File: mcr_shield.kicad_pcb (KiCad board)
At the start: 2 copper layers, 135 x 95 mm, 23 parts, among them J2 MCR_P1_Controls, J3 MCR_System_Coin, J4 MCR_Opt_X_Dial, J5 MCR_P2_Controls, SW1 Game_Selector, SW2 Cabinet_Options, U1 Buck_Regulator, U2 Optocoupler_P1, U3 Optocoupler_Sys, U4 Sync_Buffer, U5 Audio_Amplifier

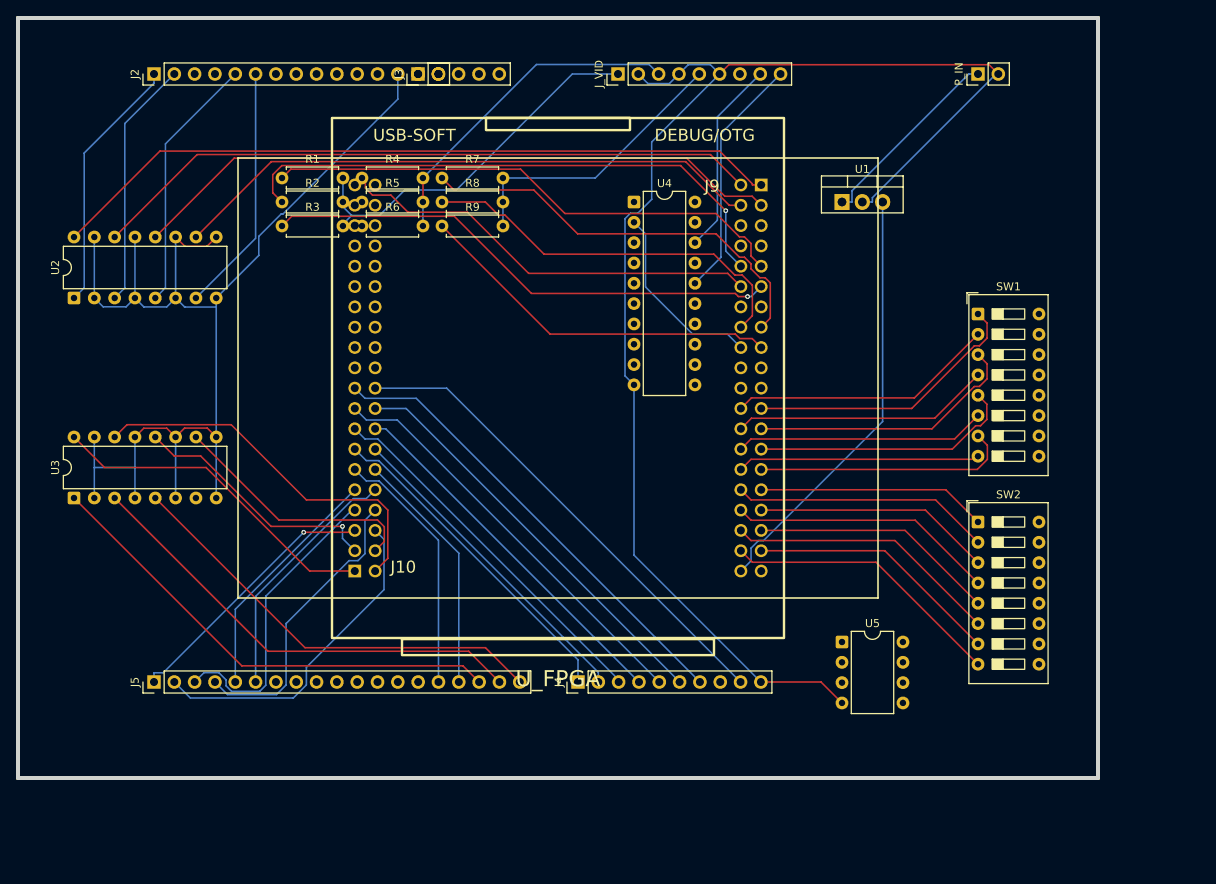
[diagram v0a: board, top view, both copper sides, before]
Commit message: Tang Console 60K bring-up: USB gamepad, multi-game configs, VGA out, DDR3 framebuffer (WIP)
Backport the working Primer 25K design to the Console 60K and grow it:

- Console 60K port verified on hardware: pins cross-checked against
  nand2mario nestang/snestang/gbatang and the Sipeed 32001A/C schematics
  (J10 header ball map extracted; docs/pinrefs/ carries the references).
- USB HID gamepad on USB port 1 (vendored nand2mario usb_hid_host + 12MHz
  PLLA); board keys act as reset/coin.
- Per-game build configs via merge_roms.py-generated game_config.vh:
  Domino Man, Tron (spinner via MiSTer spinner.sv on pad X/Y), Satan's
  Hollow - input/DIP maps verified against MAME mcr.cpp (incl. the Domino
  0x3E upright DIP fix). Flashables kept in bitstreams/.
- Analog VGA (PmodVGA or DE-15 breakout) from J10 with a 15/31kHz strap;
  PMOD-socket mapping straps pending hardware verification.
- DDR3 framebuffer HDMI path (vendored from gbatang, GPLv3): 512x480
  captured to on-SOM DDR3, upscaled to 1280x720@60 with HDMI audio.
  STATUS: builds clean, timing met, but no HDMI sync on hardware yet -
  under debug via new UART status beacon (U15 -> USB-C serial) and J10
  debug pins; gbatang-m60k reference bitstream staged as control test.
- Docs: CLAUDE.md, universal MCR shield spec (J10 pin table, net plan),
  machine-readable MCR game input matrix; Bank 9 1.5V constraint recorded.

Co-Authored-By: Claude Fable 5 <noreply@anthropic.com>
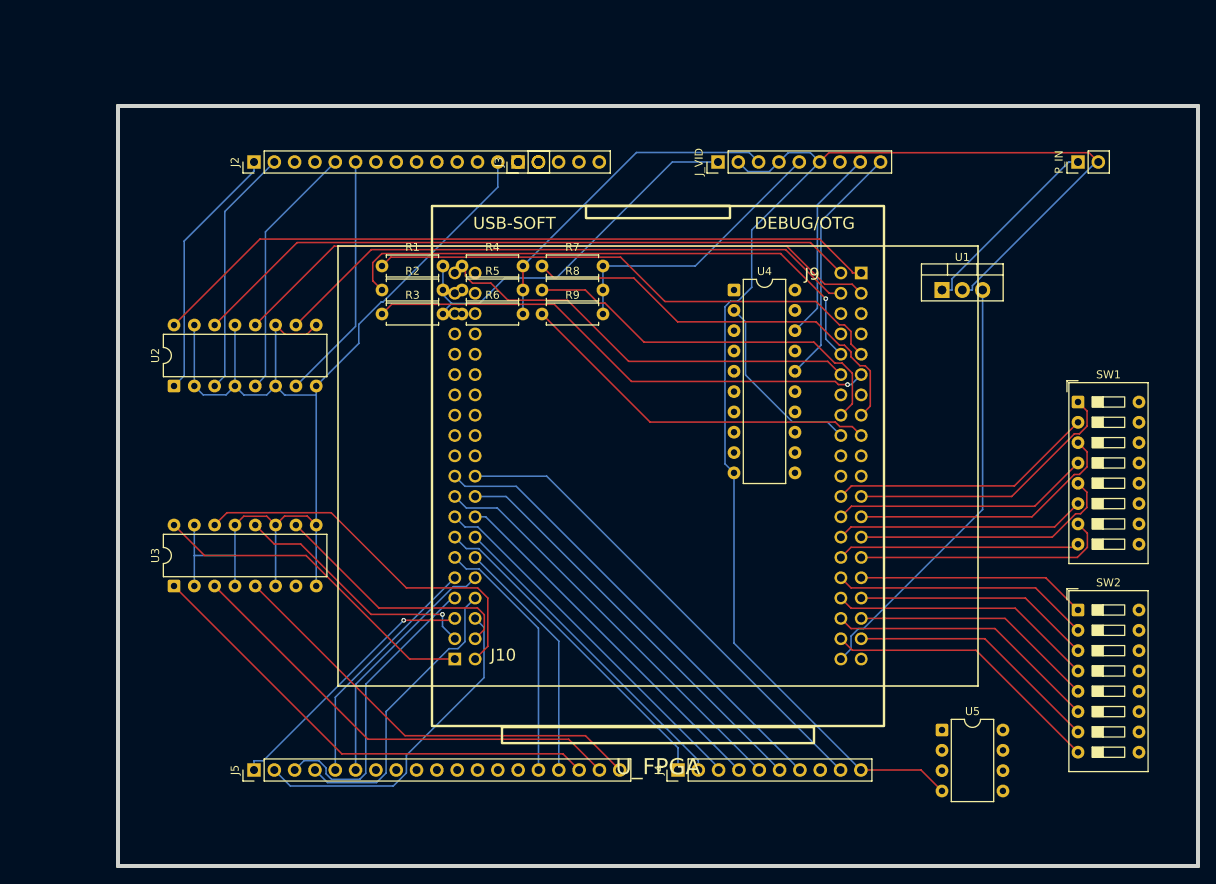
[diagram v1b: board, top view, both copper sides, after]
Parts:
- moved J2 16.7 mm to (34.5, 23.0)
- moved J3 16.7 mm to (67.5, 23.0)
- moved J4 16.7 mm to (87.5, 99.0)
- moved J5 16.7 mm to (34.5, 99.0)
- moved J_VID 16.7 mm to (92.5, 23.0)
- moved P_IN 16.7 mm to (137.5, 23.0)
- moved R1 16.7 mm to (50.5, 36.0)
- moved R2 16.7 mm to (50.5, 39.0)
- moved R3 16.7 mm to (50.5, 42.0)
- moved R4 16.7 mm to (60.5, 36.0)
- moved R5 16.7 mm to (60.5, 39.0)
- moved R6 16.7 mm to (60.5, 42.0)
- moved R7 16.7 mm to (70.5, 36.0)
- moved R8 16.7 mm to (70.5, 39.0)
- moved R9 16.7 mm to (70.5, 42.0)
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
